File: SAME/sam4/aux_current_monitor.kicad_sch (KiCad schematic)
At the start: 8 parts, among them U7 LM3480-3.3, U8 ACS71240LLCBTR-030B3

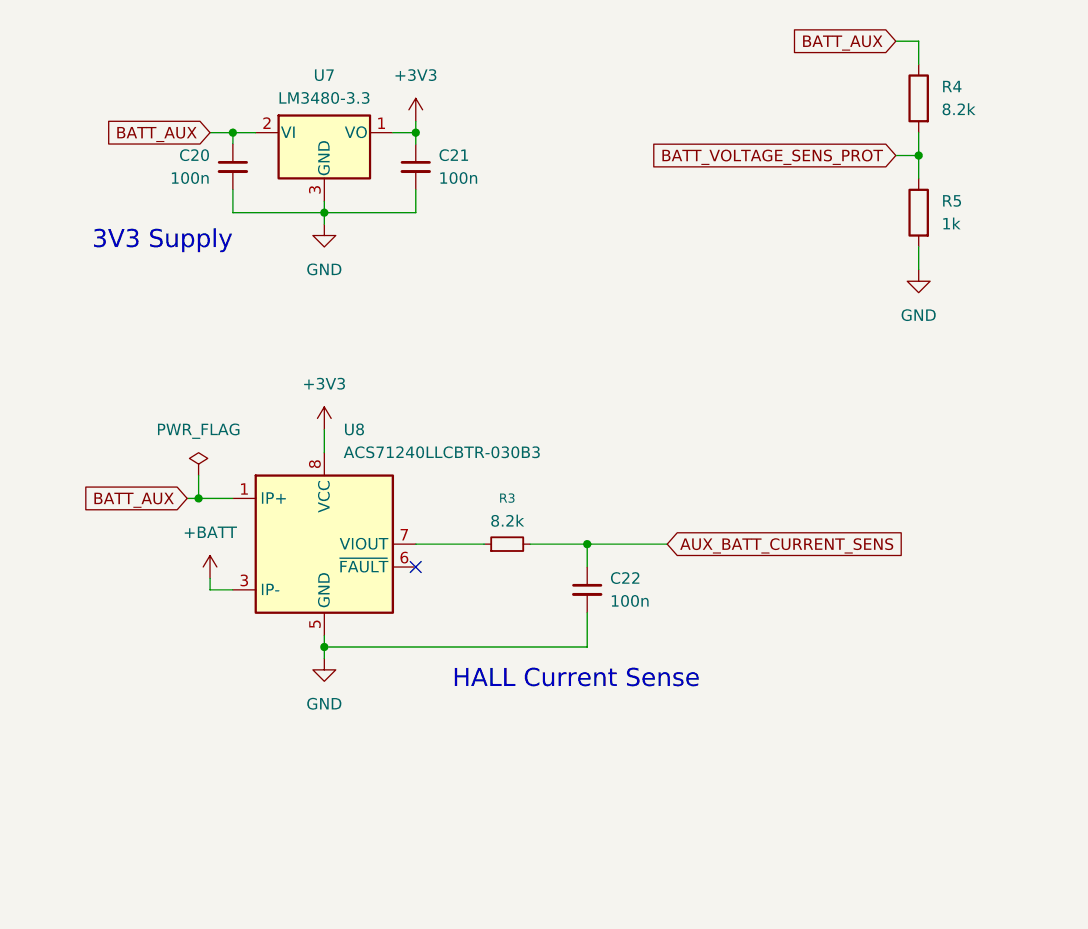
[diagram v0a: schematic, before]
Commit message: final san check routing. add protection
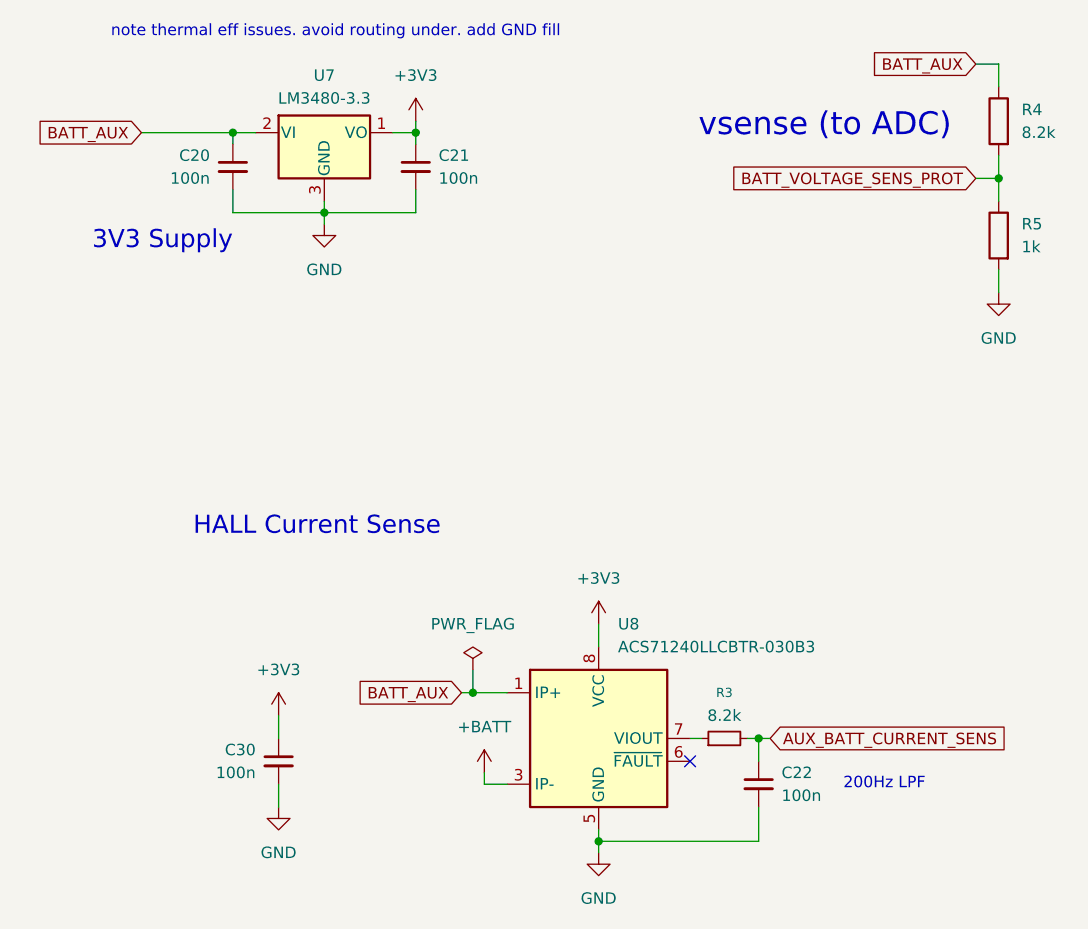
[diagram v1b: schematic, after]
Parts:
- added C30: 100n, Capacitor_SMD:C_1206_3216Metric, symbol Device:C_Small
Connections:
- net +3V3: now also C30.1
- net GND: now also C30.2
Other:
- note added: "200Hz LPF"
- note added: "note thermal eff issues. avoid routing under. add GND fill"
- note added: "vsense (to ADC)"
- moved on the sheet: C22, R3, R4, R5, U8
